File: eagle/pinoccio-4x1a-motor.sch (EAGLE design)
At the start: 27 parts, among them IC1 74LVC1G04DBV, IC2 74LVC1G04DBV, IC3 74LVC1G04DBV, IC4 74LVC1G04DBV, J1 POWER_JACKPTH, U1 TB6621FNG, U2 TB6621FNG

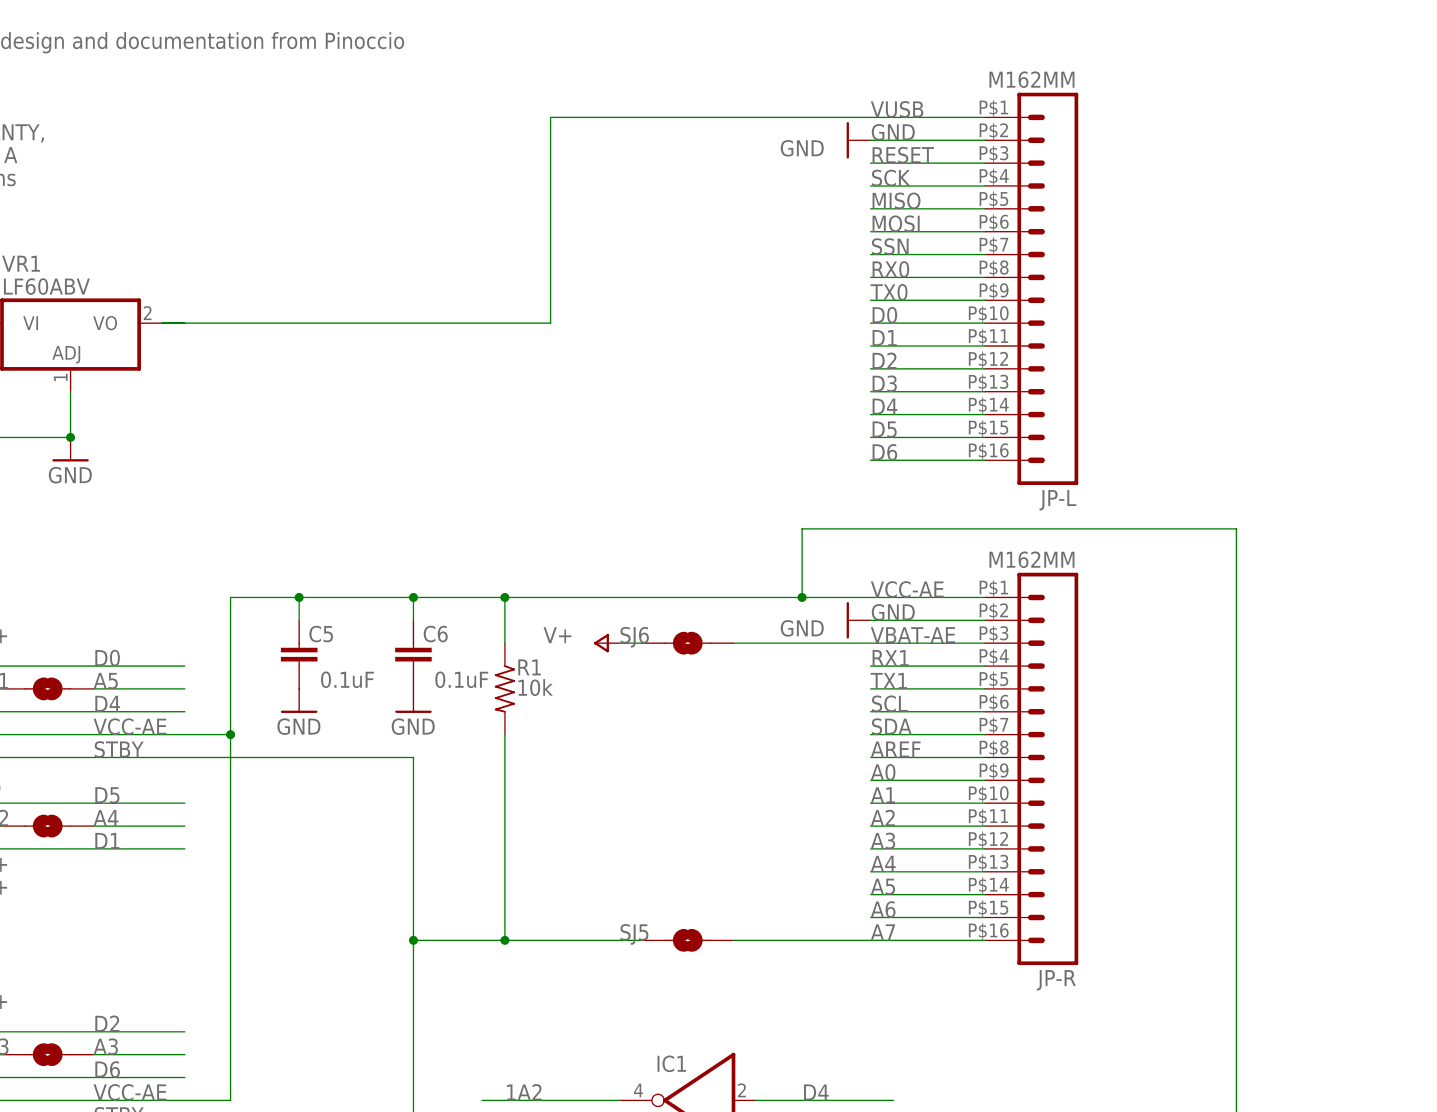
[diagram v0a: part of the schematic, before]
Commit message: Change layout onto an Arduino shield compatible board.
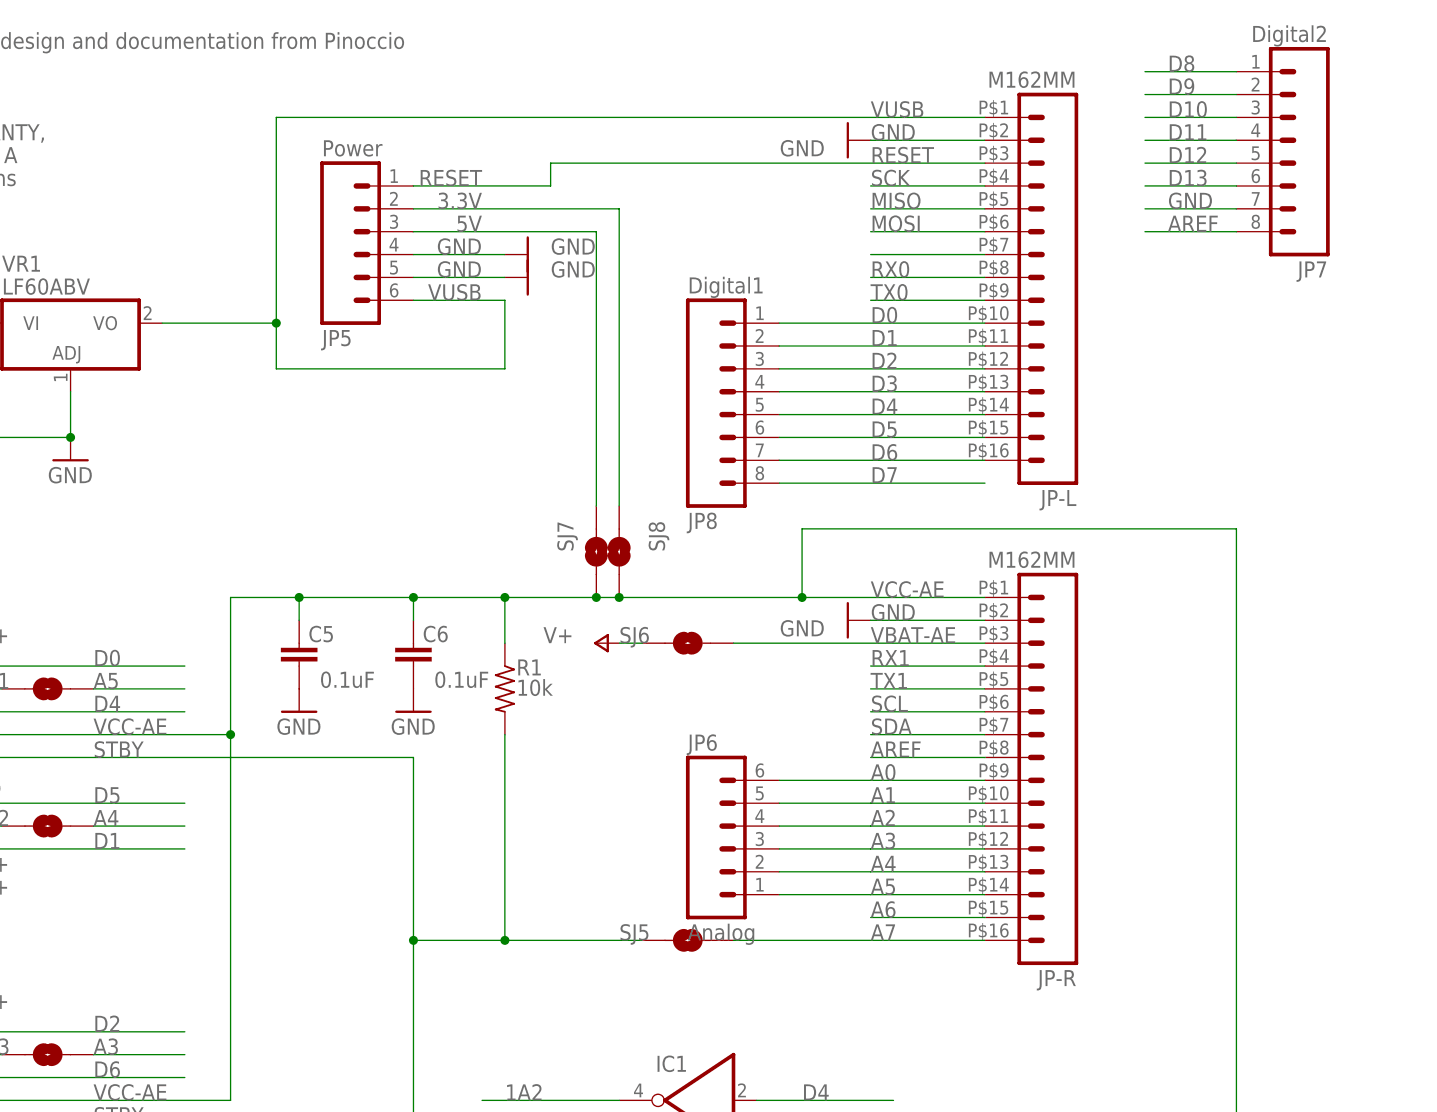
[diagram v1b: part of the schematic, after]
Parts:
- added JP5: Power, SparkFun:M06SIP
- added JP6: Analog, SparkFun:M06SIP
- added JP7: Digital2, SparkFun:M08
- added JP8: Digital1, SparkFun:M08
- added SJ7, SJ8: SOLDERJUMPERNC2, SparkFun-Passives:SOLDERJUMPERNC2
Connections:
- new net 3.3V: JP5.2, SJ8.2
- new net 5V: JP5.3, SJ7.2
- new net D10: JP7.3
- new net D11: JP7.4
- new net D12: JP7.5
- new net D13: JP7.6
- new net D7: JP8.8
- new net D8: JP7.1
- new net D9: JP7.2
- net A0: now also JP6.6
- net A1: now also JP6.5
- net A2: now also JP6.4
- net A3: now also JP6.3
- net A4: now also JP6.2
- net A5: now also JP6.1
- net AREF: now also JP7.8
- net D0: now also JP8.1
- net D1: now also JP8.2
- net D2: now also JP8.3
- net D3: now also JP8.4
- net D4: now also JP8.5
- net D5: now also JP8.6
- net D6: now also JP8.7
- net GND: now also JP5.4, JP5.5, JP7.7
- net RESET: now also JP5.1
- net VCC-AE: now also SJ7.1, SJ8.1
- net VUSB: now also JP5.6

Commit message: High current traces routed.
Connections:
- net N$8 renamed M4-
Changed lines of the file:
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@@
 </segment>
 </net>
-<net name="N$8" class="0">
+<net name="M4-" class="0">
 <segment>
 <pinref part="U2" gate="G$1" pin="B01@11"/>
